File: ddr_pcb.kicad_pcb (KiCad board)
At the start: 2 copper layers, 48.7 x 61.6 mm, 17 parts, among them J1 Screw_Terminal_01x04, J2 Screw_Terminal_01x04, J3 Screw_Terminal_01x04, J4 Screw_Terminal_01x06, J5 Screw_Terminal_01x04, U1 ProMicro

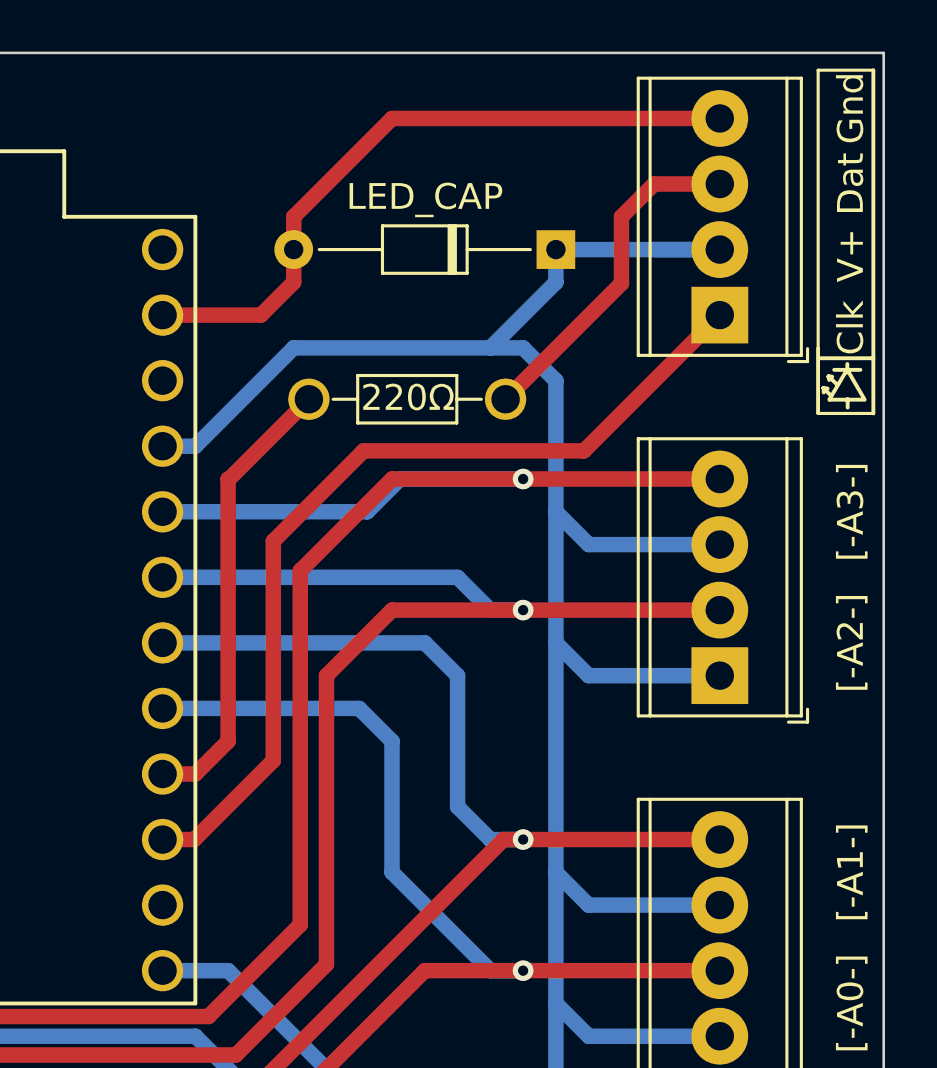
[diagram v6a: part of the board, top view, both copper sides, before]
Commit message: new: Update pins to use 15/16 for SPI. Swap Pin1 to dat for non-SPI LEDs
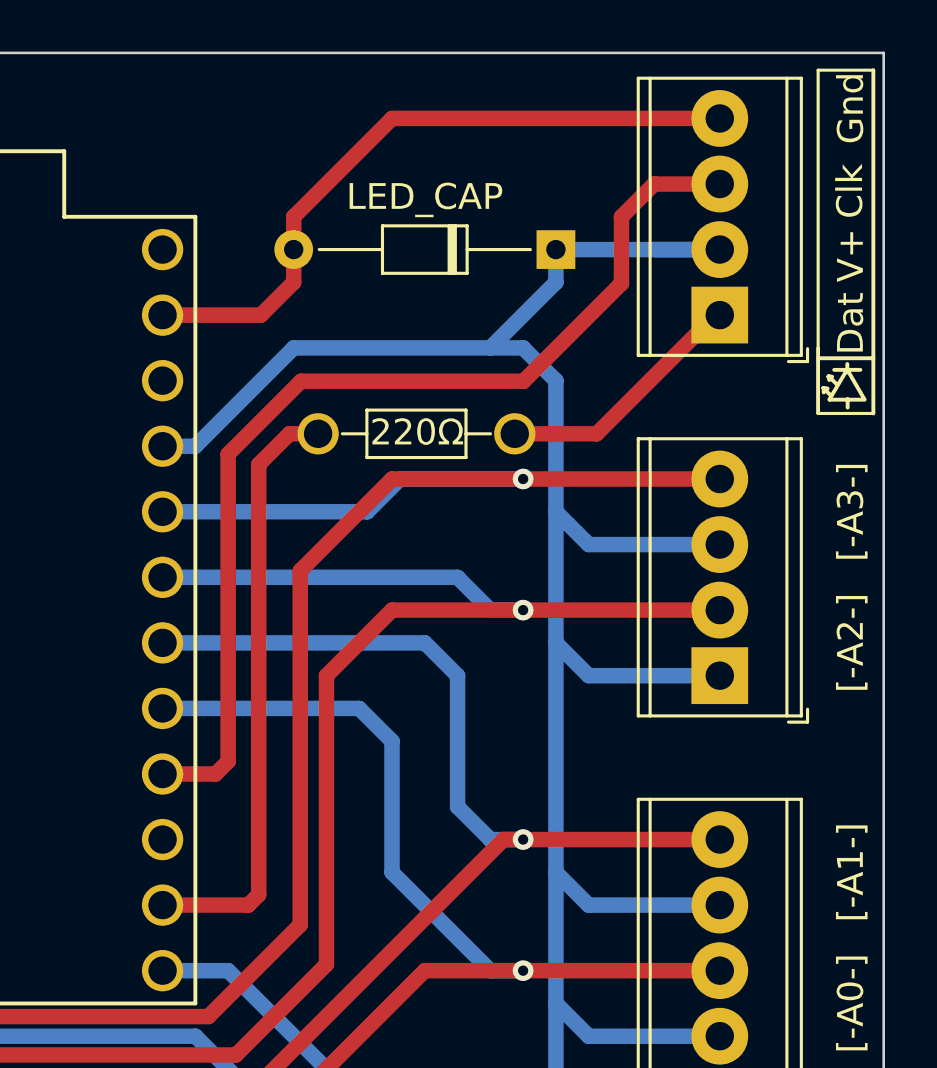
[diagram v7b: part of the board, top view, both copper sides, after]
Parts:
- moved 220Ω 1.38 mm to (106.4, 83.3)
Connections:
- J5 pad 1: Net-(J5-Pad1) -> Net-(220ohm1-Pad1)
- J5 pad 3: Net-(220ohm1-Pad1) -> Net-(J5-Pad3)
- U1 pad 14: (no net) -> Net-(220ohm1-Pad2)
- U1 pad 15: Net-(J5-Pad1) -> (no net)
- U1 pad 16: Net-(220ohm1-Pad2) -> Net-(J5-Pad3)
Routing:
- net Net-(J5-Pad3): track 0.00 -> 39.6 mm
- net Net-(J5-Pad1): track 35.0 -> 0.00 mm
- net Net-(220ohm1-Pad2): track 17.6 -> 23.4 mm
- net Net-(220ohm1-Pad1): track 13.3 -> 9.85 mm
